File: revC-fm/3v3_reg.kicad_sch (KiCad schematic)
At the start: 30 parts, among them Q1 MMDT5551-7-F, Q2 MMDT5551-7-F, Q73 MUN5311DW1, U17 INA230AIRGTR, U36 TPS54226PWPR

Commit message: almost done!!!!!
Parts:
- renumbered D5 to LED5, R68 to R41
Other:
- note added: "INPUT: VBUS 4.5-18V"
- note added: "Indicator LED"
- note added: "OUTPUT: 3.3V, ~1.5A (OCP) ~1.5A OCP (See datasheet p8 for more information.)"
- note added: "PARAMATERS"
- note added: "Power Monitor"
- note removed: "Regulator - 3.3V OUT"
- note removed: "VBUS 4.5 to 18V 8.2V Vfloat(batt charging) 7.2V Vbatt"
- note removed: "decide address"
- note removed: "~1.5A OCP (See datasheet p8 for more information.)"
- moved on the sheet: C41, C59, LED5, Q1A, Q1B, Q2A, Q2B, Q73A, Q73B, R37, R38, R39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

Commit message: updated fab files
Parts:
- C41, C52, C53, C70: Manufacturer (none) -> TDK
- C44, C45, C46: Manufacturer (none) -> Murata
- C49, C59: Manufacturer (none) -> TDK; Mfr. Part No (none) -> CGA2B3X7R1H104K050BE
- C50: Manufacturer (none) -> TDK; Mfr. Part No (none) -> CGA2B2X7R1H332K050BA
- C57: Manufacturer (none) -> TDK; Mfr. Part No (none) -> CGA3E1X7R1V105K080AE
- L3: Manufacturer (none) -> Würth Elektronik
- LED5: Manufacturer (none) -> Kingbright; Mfr. Part No (none) -> APHHS1005LSYCK/J3-PF
- Q1, Q2: Manufacturer (none) -> Diodes Incorporated; Mfr. Part No (none) -> MMDT5551-7-F
- Q73: Manufacturer (none) -> onsemi; Mfr. Part No (none) -> MUN5311DW1
- R37, R49: Manufacturer (none) -> Stackpole Electronics; Mfr. Part No (none) -> RMCF0603FT73K2
- R38, R40, R47: Manufacturer (none) -> Stackpole Electronics; Mfr. Part No (none) -> RMCF0402FT100K
- R39: Manufacturer (none) -> Stackpole Electronics; Mfr. Part No (none) -> RMCF0402FT200K
- R41: value 1.8k -> 1.5k; Manufacturer (none) -> Stackpole Electronics; Mfr. Part No (none) -> RMCF0402FT1K50
- R42: Manufacturer (none) -> Stackpole Electronics; Mfr. Part No (none) -> RMCF0402FT10K0
- R44: Manufacturer (none) -> Stackpole Electronics; Mfr. Part No (none) -> RMCF0402FT20K0
- R50: Manufacturer (none) -> Stackpole Electronics; Mfr. Part No (none) -> RMCF0603FT22K1
- R56: footprint Resistor_SMD:R_1210_3225Metric -> Resistor_SMD:R_1206_3216Metric; Manufacturer (none) -> Vishay Dale; Mfr. Part No (none) -> WSLP1206R0100
- U17: Manufacturer (none) -> Texas Instruments
- U22: renamed from U36; Manufacturer (none) -> Texas Instruments; Mfr. Part No (none) -> TPS54226PWPR

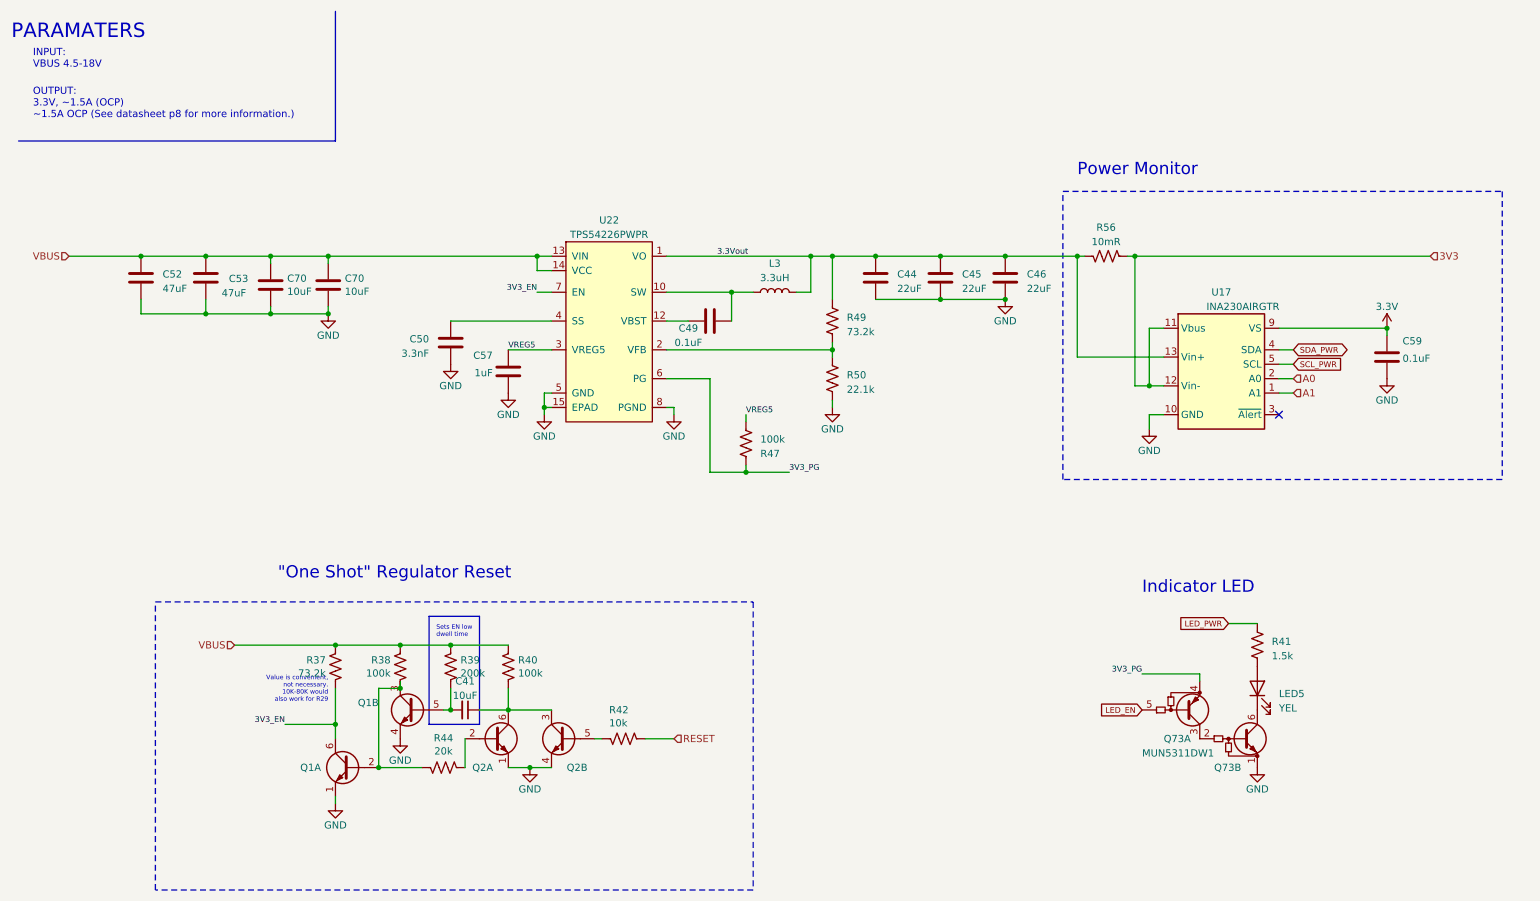
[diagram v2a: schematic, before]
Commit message: updated per review, improved docs
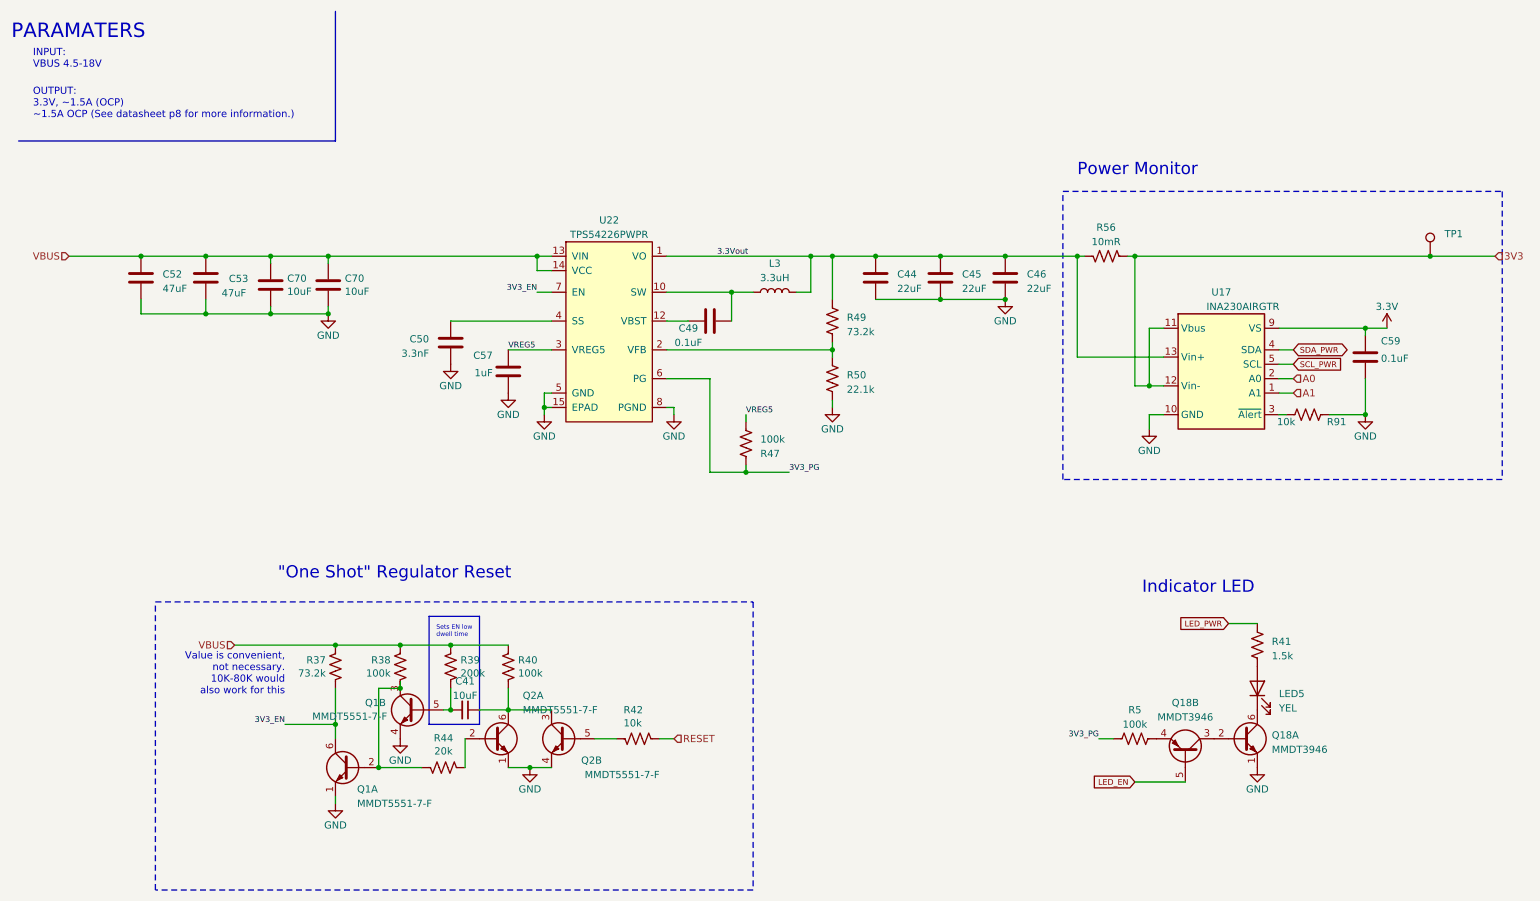
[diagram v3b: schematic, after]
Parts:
- removed Q73: MUN5311DW1, Package_TO_SOT_SMD:SOT-363_SC-70-6, symbol SierraLobo:MUN5312DW1
- added Q18: MMDT3946, Package_TO_SOT_SMD:SOT-363_SC-70-6, symbol Transistor_BJT:MMDT3946
- added R5: 100k, Resistor_SMD:R_0402_1005Metric, symbol Device:R_US
- added R91: 10k, Resistor_SMD:R_0402_1005Metric, symbol Device:R_US
- added TP1: RCU-0C, SierraLobo:TestPoint_TE_RCU_0603, symbol Connector:TestPoint
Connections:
- net 3V3: now also TP1.1
- net 3V3_PG: now also R5.2
- net EP: now also Q18.1 (E1), R91.1
- net LED_EN: now also Q18.5 (B2)
- net at LED5.1 (K): now also Q18.6 (C1)
- net at U17.3 (~{Alert}): now also R91.2
- new net: Q18.2 (B1), Q18.3 (C2)
- new net: Q18.4 (E2), R5.1
- no-connect marks 1 -> 0
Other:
- note added: "Value is convenient, not necessary. 10K-80K would also work for this"
- note removed: "Value is convenient, not necessary. 10K-80K would also work for R29"
- moved on the sheet: C59, R42
